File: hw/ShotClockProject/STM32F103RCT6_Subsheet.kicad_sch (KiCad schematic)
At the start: 35 parts, among them J1 Conn_01x04_Pin, J3 Conn_01x06_Pin, P1 USB_C_Plug_USB2.0, Q2 Q_NPN_BCE, SW1 SW_SPDT, U1 STM32F103RCT6, Y1 16MHz

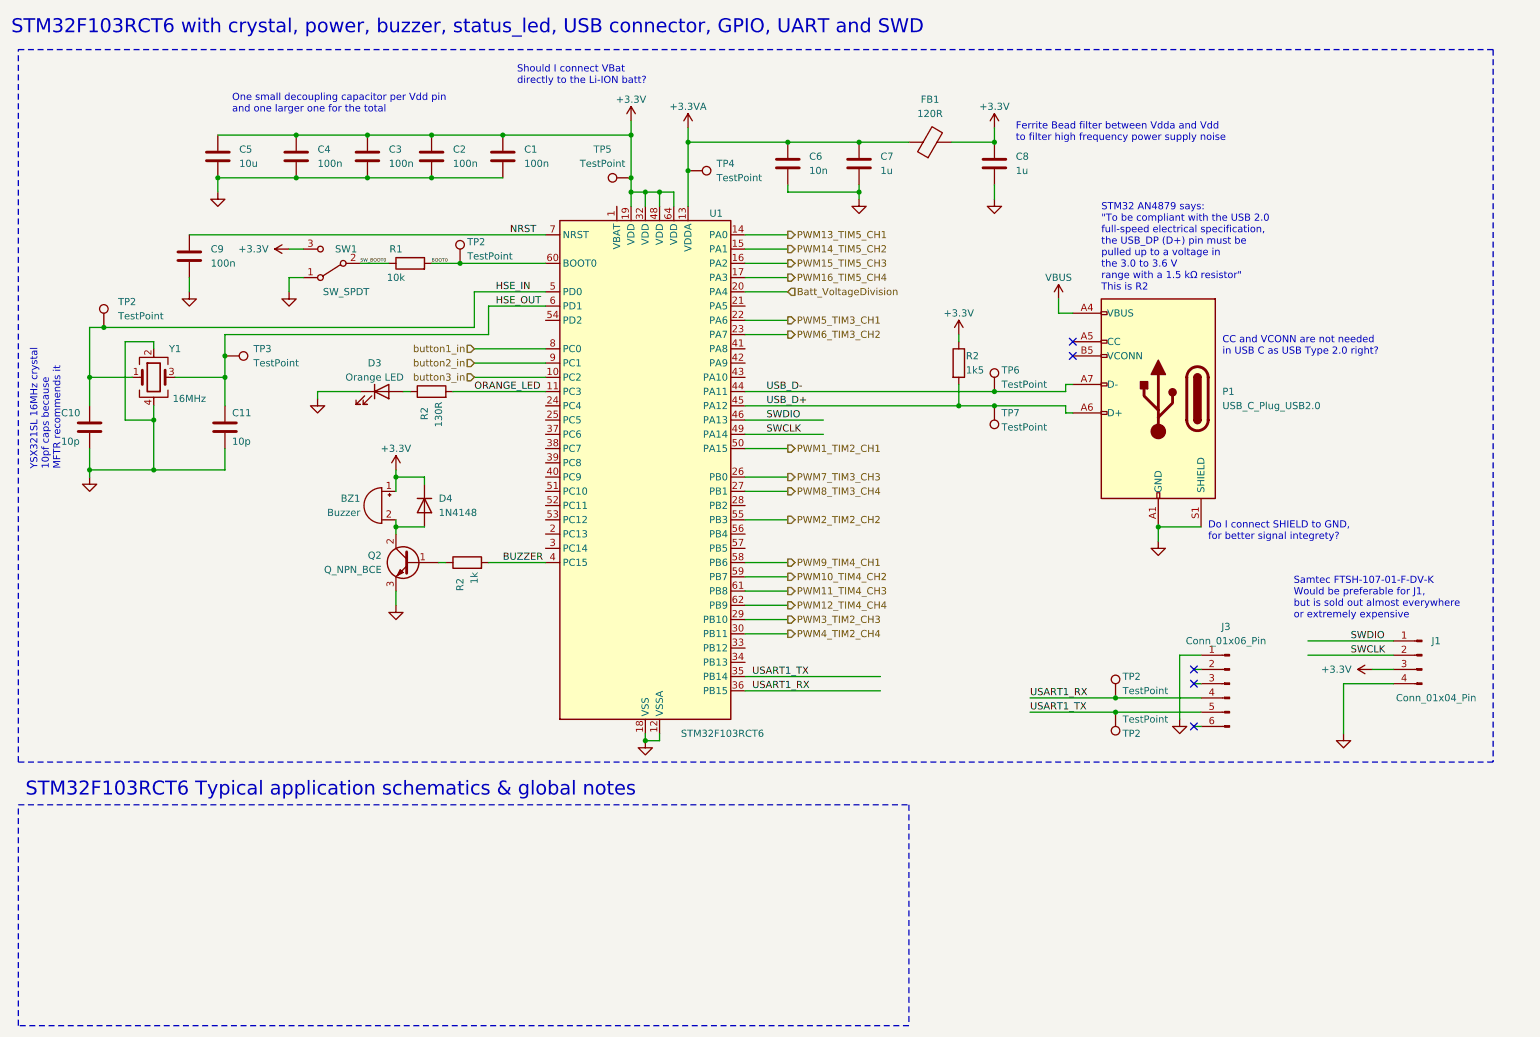
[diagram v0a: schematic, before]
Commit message: Changed documentation, added to schematics
Added Vbat connection via LDO
Added jumper to enable/disable the TEMP pin of chrg IC.
Added PDF exports of schematics
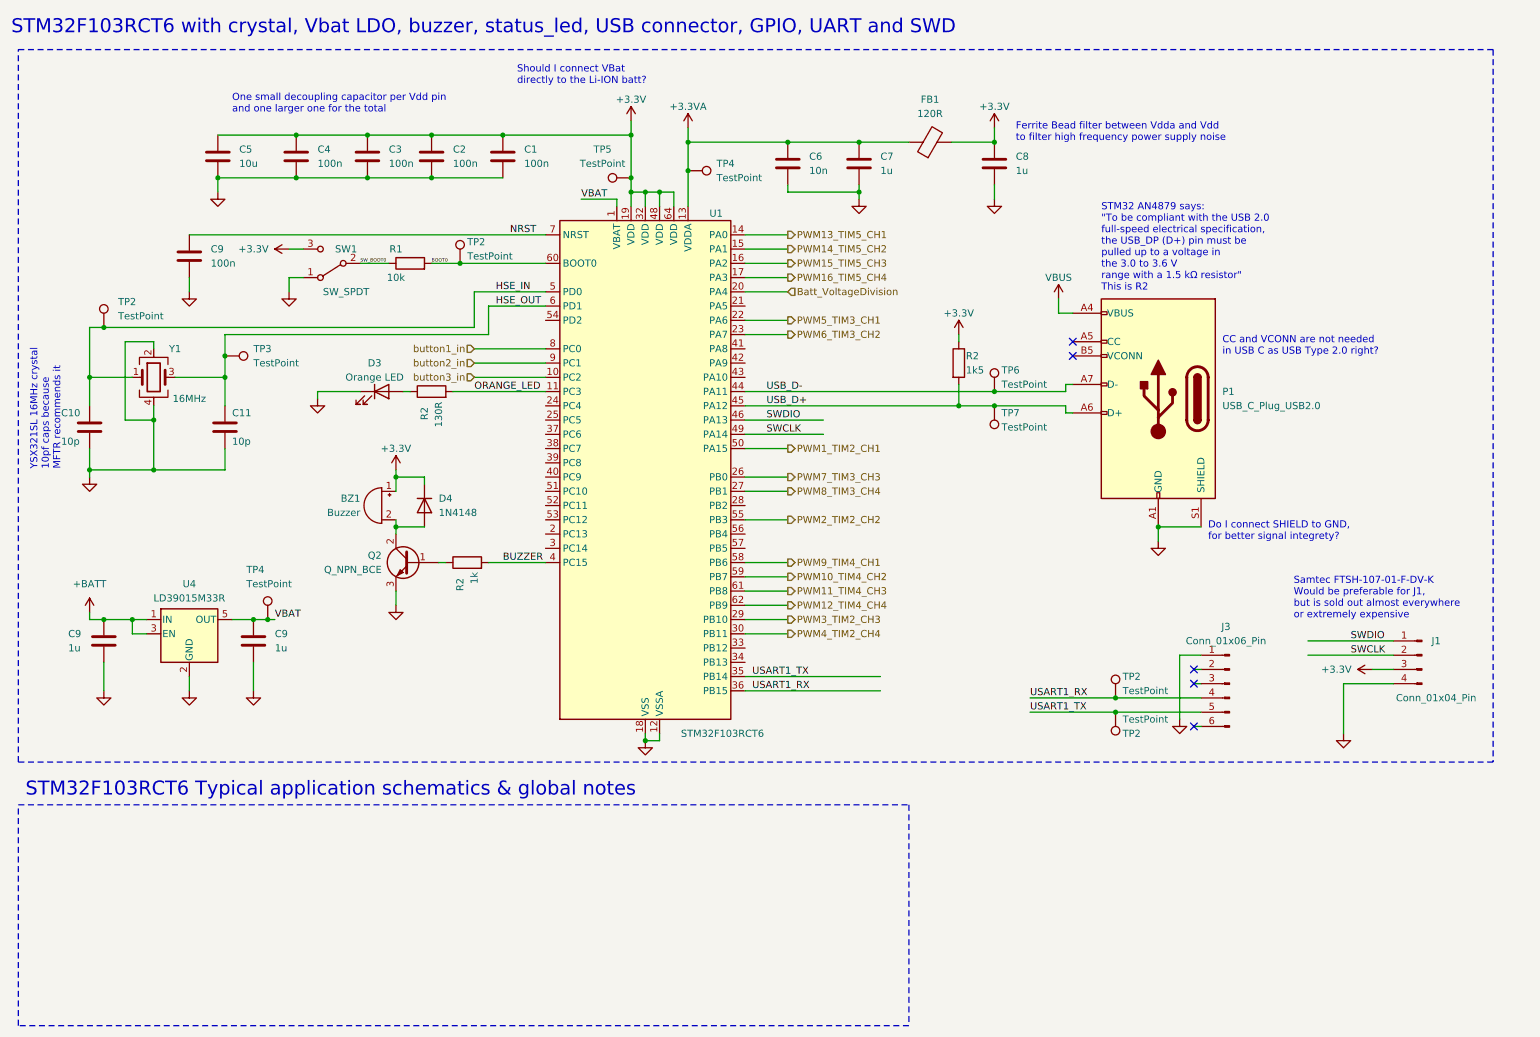
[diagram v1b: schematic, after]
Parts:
- added C9 (x2): 1u, symbol Device:C
- added TP4: TestPoint, symbol Connector:TestPoint
- added U4: LD39015M33R, Package_TO_SOT_SMD:SOT-23-5, symbol Regulator_Linear:LD39015M33R
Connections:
- net GND: now also C9.2, C9.2, U4.2 (GND)
- net VBAT: now reaches U1.1 (VBAT)
- net VBAT: now also C9.1, TP4.1, U4.5 (OUT)
- new net +BATT: C9.1, U4.1 (IN), U4.3 (EN)
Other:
- note added: "STM32F103RCT6 with crystal, Vbat LDO, buzzer, status_led, USB connector, GPIO, UART and SWD"
- note removed: "STM32F103RCT6 with crystal, power, buzzer, status_led, USB connector, GPIO, UART and SWD"

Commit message: Fixed all ERC issues
Mainly by placing PWR_FLAGs and NetTies to show KiCAD where the GNDs are connected to each other physically, without them being the same net.
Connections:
- no-connect marks 5 -> 26
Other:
- note added: "PWR_FLAG to tell KiCAD where all the power outputs come from. GND is chosen here, since my 'src GND' is actually Batt-"
- note removed: "Should I connect VBat directly to the Li-ION batt?"

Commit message: Init of SW, changes on HW
SW init STMIDE project
HW Added first few footprints for passive components.
Removed old name .IOC file
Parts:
- removed TP2 (x2): TestPoint, symbol Connector:TestPoint
- added J10: Conn_ST_STDC14, Connector_PinHeader_1.27mm:PinHeader_2x07_P1.27mm_Vertical_SMD, symbol Connector:Conn_ST_STDC14
- C1, C10, C11, C2, C3, C4, C6, C7, C8, C9: footprint (none) -> Capacitor_SMD:C_0402_1005Metric
- C5: footprint (none) -> Capacitor_SMD:C_0603_1608Metric
- D3: footprint (none) -> LED_SMD:LED_0603_1608Metric
- FB1: footprint (none) -> Inductor_SMD:L_0603_1608Metric
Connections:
- net +3.3V: now also J10.3 (VCC)
- net GND: now also J10.5 (GND), J10.7 (GND)
- net SWCLK: now also J10.6 (JCLK/SWCLK)
- net SWDIO: now also J10.4 (JTMS/SWDIO)
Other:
- note removed: "Samtec FTSH-107-01-F-DV-K Would be preferable for J1, but is sold out almost everywhere or extremely expensive"
- moved on the sheet: J1, J3

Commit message: Finished footprint selection & updated design doc
Chosen all footprints
Updated design doc with part link & part selection reasons
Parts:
- removed J1: Conn_01x04_Pin, symbol Connector:Conn_01x04_Pin
- removed P1: USB_C_Plug_USB2.0, symbol Connector:USB_C_Plug_USB2.0
- added J1: USB_C_Receptacle_USB2.0, Connector_USB:USB_C_Receptacle_Molex_105450-0101, symbol Connector:USB_C_Receptacle_USB2.0
- added R2: 100R, Resistor_SMD:R_0603_1608Metric, symbol Device:R
- added R2 (x2): 5k1, Resistor_SMD:R_0603_1608Metric, symbol Device:R
- BZ1: footprint (none) -> Buzzer_Beeper:Buzzer_CUI_CPT-9019S-SMT
- C1, C10, C11, C2, C3, C4, C6, C7, C8, C9: footprint Capacitor_SMD:C_0402_1005Metric -> Capacitor_SMD:C_0603_1608Metric
- D4: footprint Diode_THT:D_DO-35_SOD27_P7.62mm_Horizontal -> Diode_SMD:D_SOD-323
- J3: footprint (none) -> Connector_PinHeader_2.54mm:PinHeader_1x06_P2.54mm_Vertical_SMD_Pin1Left
- Q2: footprint (none) -> Package_TO_SOT_SMD:SOT-23
- R1, R2: footprint (none) -> Resistor_SMD:R_0603_1608Metric
- SW1: footprint (none) -> Button_Switch_SMD:SW_SPST_B3U-1000P
- TP2, TP3, TP4, TP5, TP6, TP7: footprint (none) -> TestPoint:TestPoint_Pad_D2.5mm
- Y1: footprint (none) -> Crystal:Crystal_SMD_3225-4Pin_3.2x2.5mm
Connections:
- net GND: now also J1.A1 (GND), J1.A12 (GND), J1.B1 (GND), J1.B12 (GND), J1.S1 (SHIELD), R2.2, R2.2, R2.2
- net NRST: now also J10.12 (~{RST})
- net USB_D+: now also J1.A6 (D+), J1.B6 (D+)
- net USB_D-: now also J1.A7 (D-), J1.B7 (D-)
- net VBUS: now also J1.A4 (VBUS), J1.A9 (VBUS), J1.B4 (VBUS), J1.B9 (VBUS)
- net at J10.11 (GNDDetect): now also R2.1
- new net: J1.A5 (CC1), R2.1
- new net: J1.B5 (CC2), R2.1
- no-connect marks 26 -> 31
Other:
- note added: "X322516MMB4SI 16MHz crystal 10pf caps because MFTR recommends it"
- note removed: "CC and VCONN are not needed in USB C as USB Type 2.0 right?"
- note removed: "YSX321SL 16MHz crystal 10pf caps because MFTR recommends it"
- moved on the sheet: J10, J3, R2, TP6, TP7

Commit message: HW changes
Changed Switches to correct SPDT instead of SPST.
Added design requirements to PCB according to JLCPCB specs
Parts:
- SW1: footprint Button_Switch_SMD:SW_SPST_B3U-1000P -> Button_Switch_SMD:SW_SPDT_PCM12
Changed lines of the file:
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@@
       (effects (font (size 1.27 1.27)))
     )
-    (property "Footprint" "Button_Switch_SMD:SW_SPST_B3U-1000P" (at 71.12 59.69 0)
+    (property "Footprint" "Button_Switch_SMD:SW_SPDT_PCM12" (at 71.12 59.69 0)
       (effects (font (size 1.27 1.27)) hide)
     )

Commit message: Renamed references
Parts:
- renumbered D3 to D1, D4 to D2, J10 to J2, Q2 to Q1, U4 to U2

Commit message: Changed footprint
To horizontal 2.54 connectors
and started on rough layout
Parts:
- C1, C10, C11, C2, C3, C4, C6, C7, C8, C9: footprint Capacitor_SMD:C_0603_1608Metric -> Capacitor_SMD:C_0402_1005Metric
- J2: footprint Connector_PinHeader_1.27mm:PinHeader_2x07_P1.27mm_Vertical_SMD -> Connector_PinHeader_1.27mm:PinHeader_2x07_P1.27mm_Horizontal
- J3: footprint Connector_PinHeader_2.54mm:PinHeader_1x06_P2.54mm_Vertical_SMD_Pin1Left -> Connector_PinHeader_2.54mm:PinHeader_1x06_P2.54mm_Horizontal
- R1, R2: footprint Resistor_SMD:R_0603_1608Metric -> Resistor_SMD:R_0402_1005Metric
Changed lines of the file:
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@@
       (effects (font (size 1.27 1.27)) (justify left))
     )
-    (property "Footprint" "Capacitor_SMD:C_0603_1608Metric" (at 58.1152 130.81 0)
+    (property "Footprint" "Capacitor_SMD:C_0402_1005Metric" (at 58.1152 130.81 0)
       (effects (font (size 1.27 1.27)) hide)
     )
@@
       (effects (font (size 1.27 1.27)) (justify left))
     )
-    (property "Footprint" "Capacitor_SMD:C_0603_1608Metric" (at 89.8652 44.45 0)
+    (property "Footprint" "Capacitor_SMD:C_0402_1005Metric" (at 89.8652 44.45 0)
       (effects (font (size 1.27 1.27)) hide)
     )
@@
       (effects (font (size 1.27 1.27)) (justify left))
     )
-    (property "Footprint" "Capacitor_SMD:C_0603_1608Metric" (at 31.4452 130.81 0)
+    (property "Footprint" "Capacitor_SMD:C_0402_1005Metric" (at 31.4452 130.81 0)
       (effects (font (size 1.27 1.27)) hide)
     )
@@
       (effects (font (size 1.27 1.27)) (justify left))
     )
-    (property "Footprint" "Capacitor_SMD:C_0603_1608Metric" (at 190.1952 45.72 0)
+    (property "Footprint" "Capacitor_SMD:C_0402_1005Metric" (at 190.1952 45.72 0)
       (effects (font (size 1.27 1.27)) hide)
     )
@@
       (effects (font (size 1.27 1.27)) (justify left))
     )
-    (property "Footprint" "Capacitor_SMD:C_0603_1608Metric" (at 166.0652 45.72 0)
+    (property "Footprint" "Capacitor_SMD:C_0402_1005Metric" (at 166.0652 45.72 0)
       (effects (font (size 1.27 1.27)) hide)
     )
@@
       (effects (font (size 1.27 1.27)) (justify left))
     )
-    (property "Footprint" "Resistor_SMD:R_0603_1608Metric" (at 266.192 151.13 90)
+    (property "Footprint" "Resistor_SMD:R_0402_1005Metric" (at 266.192 151.13 90)
       (effects (font (size 1.27 1.27)) hide)
     )
@@
       (effects (font (size 1.27 1.27)) (justify left))
     )
-    (property "Footprint" "Capacitor_SMD:C_0603_1608Metric" (at 28.9052 92.71 0)
+    (property "Footprint" "Capacitor_SMD:C_0402_1005Metric" (at 28.9052 92.71 0)
       (effects (font (size 1.27 1.27)) hide)
     )
@@
       (effects (font (size 1.27 1.27)) (justify left))
     )
-    (property "Footprint" "Capacitor_SMD:C_0603_1608Metric" (at 78.4352 44.45 0)
+    (property "Footprint" "Capacitor_SMD:C_0402_1005Metric" (at 78.4352 44.45 0)
       (effects (font (size 1.27 1.27)) hide)
     )
@@
       (effects (font (size 1.27 1.27)) (justify left))
     )
-    (property "Footprint" "Resistor_SMD:R_0603_1608Metric" (at 88.9 84.328 90)
+    (property "Footprint" "Resistor_SMD:R_0402_1005Metric" (at 88.9 84.328 90)
       (effects (font (size 1.27 1.27)) hide)
     )
@@
       (effects (font (size 1.27 1.27)) (justify left))
     )
-    (property "Footprint" "Resistor_SMD:R_0603_1608Metric" (at 95.25 114.808 90)
+    (property "Footprint" "Resistor_SMD:R_0402_1005Metric" (at 95.25 114.808 90)
       (effects (font (size 1.27 1.27)) hide)
     )
@@
       (effects (font (size 1.27 1.27)) (justify left))
     )
-    (property "Footprint" "Resistor_SMD:R_0603_1608Metric" (at 214.122 60.96 90)
+    (property "Footprint" "Resistor_SMD:R_0402_1005Metric" (at 214.122 60.96 90)
       (effects (font (size 1.27 1.27)) hide)
     )
@@
       (effects (font (size 1.27 1.27)) (justify left))
     )
-    (property "Footprint" "Capacitor_SMD:C_0603_1608Metric" (at 102.5652 44.45 0)
+    (property "Footprint" "Capacitor_SMD:C_0402_1005Metric" (at 102.5652 44.45 0)
       (effects (font (size 1.27 1.27)) hide)
     )
@@
       (effects (font (size 1.27 1.27)))
     )
-    (property "Footprint" "Connector_PinHeader_2.54mm:PinHeader_1x06_P2.54mm_Vertical_SMD_Pin1Left" (at 231.14 148.59 0)
+    (property "Footprint" "Connector_PinHeader_2.54mm:PinHeader_1x06_P2.54mm_Horizontal" (at 231.14 148.59 0)
       (effects (font (size 1.27 1.27)) hide)
     )
@@
       (effects (font (size 1.27 1.27)) (justify right))
     )
-    (property "Footprint" "Connector_PinHeader_1.27mm:PinHeader_2x07_P1.27mm_Vertical_SMD" (at 265.43 128.27 0)
+    (property "Footprint" "Connector_PinHeader_1.27mm:PinHeader_2x07_P1.27mm_Horizontal" (at 265.43 128.27 0)
       (effects (font (size 1.27 1.27)) hide)
     )
@@
       (effects (font (size 1.27 1.27)) (justify left))
     )
-    (property "Footprint" "Capacitor_SMD:C_0603_1608Metric" (at 65.7352 44.45 0)
+    (property "Footprint" "Capacitor_SMD:C_0402_1005Metric" (at 65.7352 44.45 0)
       (effects (font (size 1.27 1.27)) hide)
     )
@@
       (effects (font (size 1.27 1.27)) (justify left))
     )
-    (property "Footprint" "Resistor_SMD:R_0603_1608Metric" (at 228.6 59.182 90)
+    (property "Footprint" "Resistor_SMD:R_0402_1005Metric" (at 228.6 59.182 90)
       (effects (font (size 1.27 1.27)) hide)
     )
@@
       (effects (font (size 1.27 1.27)) (justify left))
     )
-    (property "Footprint" "Capacitor_SMD:C_0603_1608Metric" (at 153.3652 45.72 0)
+    (property "Footprint" "Capacitor_SMD:C_0402_1005Metric" (at 153.3652 45.72 0)
       (effects (font (size 1.27 1.27)) hide)
     )
@@
       (effects (font (size 1.27 1.27)) (justify left))
     )
-    (property "Footprint" "Capacitor_SMD:C_0603_1608Metric" (at 53.0352 92.71 0)
+    (property "Footprint" "Capacitor_SMD:C_0402_1005Metric" (at 53.0352 92.71 0)
       (effects (font (size 1.27 1.27)) hide)
     )
@@
       (effects (font (size 1.27 1.27)) (justify left))
     )
-    (property "Footprint" "Capacitor_SMD:C_0603_1608Metric" (at 46.6852 62.23 0)
+    (property "Footprint" "Capacitor_SMD:C_0402_1005Metric" (at 46.6852 62.23 0)
       (effects (font (size 1.27 1.27)) hide)
     )
@@
       (effects (font (size 1.27 1.27)))
     )
-    (property "Footprint" "Resistor_SMD:R_0603_1608Metric" (at 85.09 61.468 90)
+    (property "Footprint" "Resistor_SMD:R_0402_1005Metric" (at 85.09 61.468 90)
       (effects (font (size 1.27 1.27)) hide)
     )
@@
       (effects (font (size 1.27 1.27)) (justify left))
     )
-    (property "Footprint" "Resistor_SMD:R_0603_1608Metric" (at 228.6 56.642 90)
-      (effects (font (size 1.27 1.27)) hide)
-    )
+    (property "Footprint" "Resistor_SMD:R_0402_1005Metric" (at 228.6 56.642 90)
+      (effects (font (size 1.27 1.27)) hide)
+    )
